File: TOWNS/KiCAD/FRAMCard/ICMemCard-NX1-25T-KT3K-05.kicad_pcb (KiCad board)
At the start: 2 copper layers, 78.5 x 47.2 mm, 19 parts, among them J1 PCMCIA_Connector, Q1 BC846X, Q2 BC846X, U1 FM18W08-SGTR, U2 FM18W08-SGTR, U3 SN74LS32DR

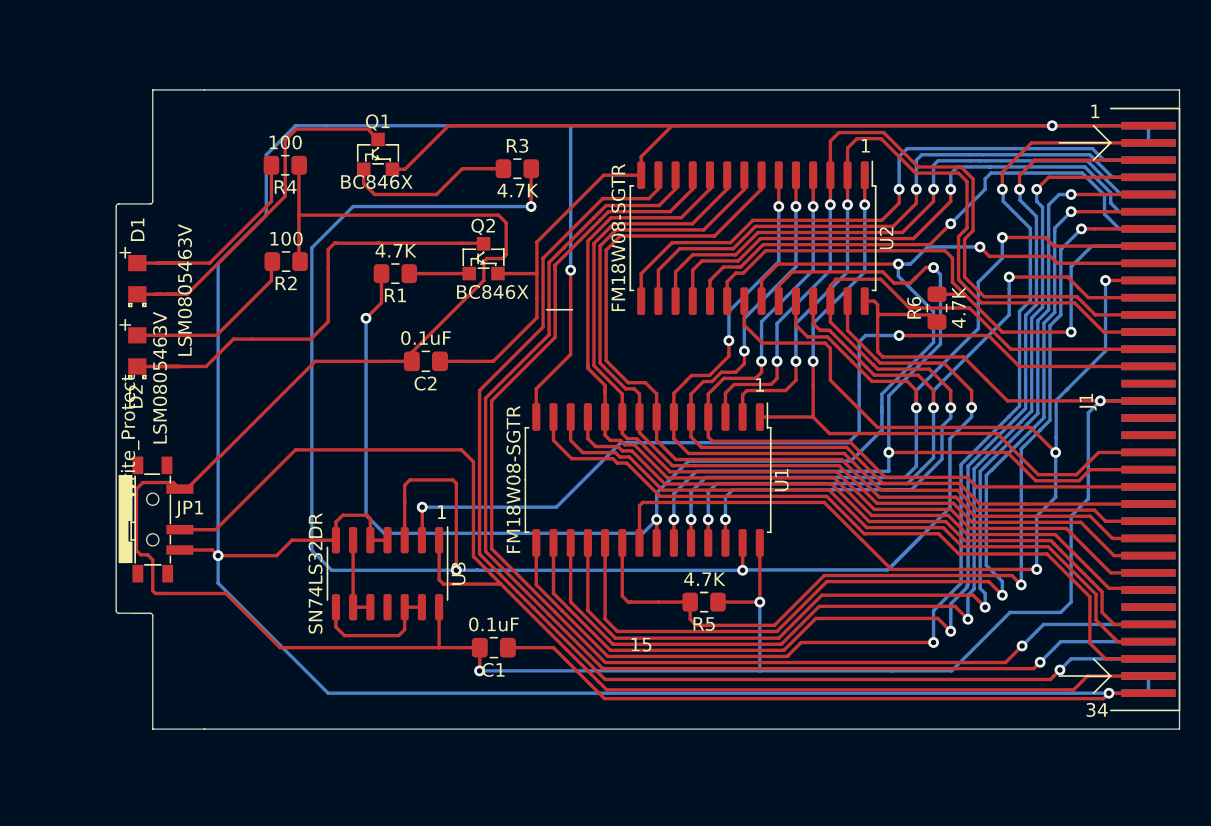
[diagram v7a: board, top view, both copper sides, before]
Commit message: Simplifying PCB
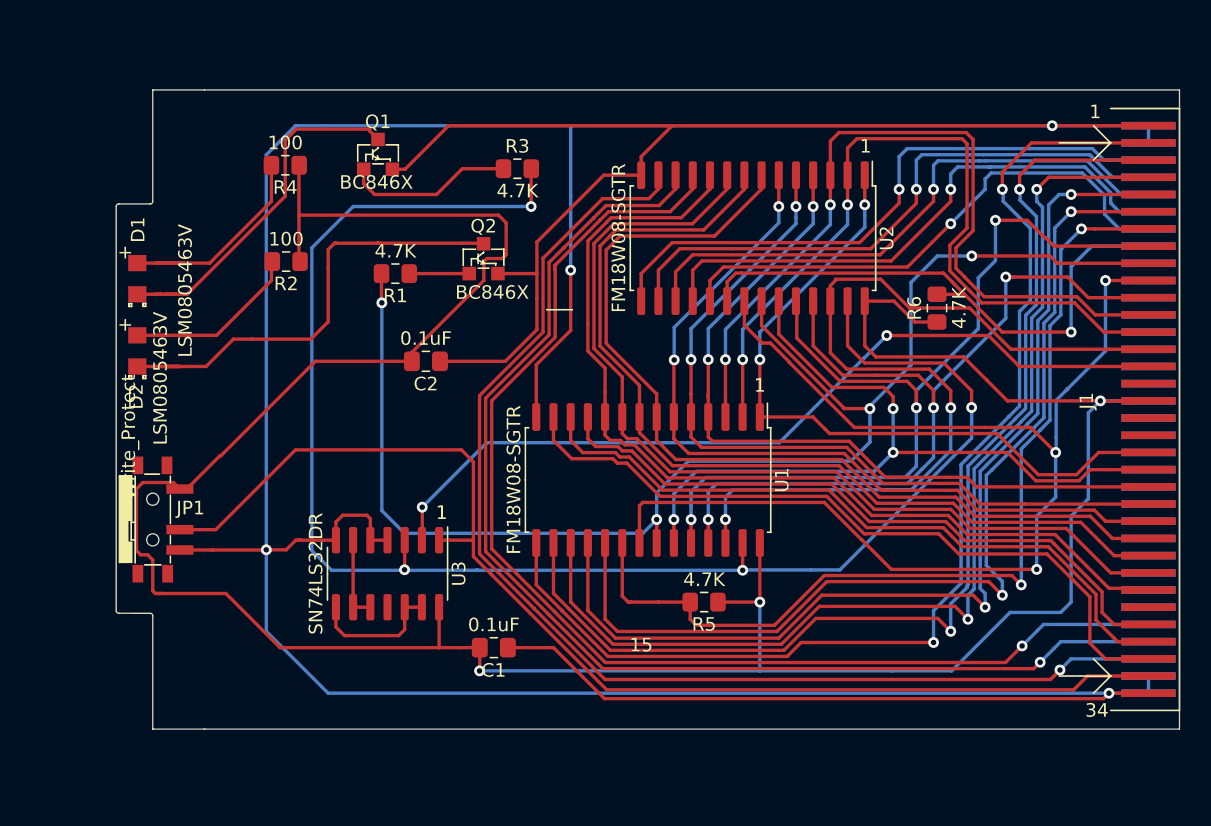
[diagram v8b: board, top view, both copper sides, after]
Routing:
- net /~WE~orWP: track 134.3 -> 117.7 mm
- net /A12: track 71.5 -> 58.0 mm
- net /~OE: track 110.0 -> 103.9 mm
- net /WP: track 93.5 -> 88.4 mm
- net /~WE: track 66.3 -> 62.4 mm
- net /A10: track 65.7 -> 68.3 mm
- net /~CE2: track 44.5 -> 42.1 mm
- net GND: track 353.1 -> 350.8 mm
- net /A15: track 50.6 -> 52.2 mm
- net /A11: track 91.1 -> 89.7 mm
- net /A14: track 65.4 -> 66.8 mm
- net Vcc: track 208.6 -> 209.8 mm
- net /A7: track 57.9 -> 56.8 mm
- net /A6: track 59.5 -> 58.5 mm
- net /A5: track 61.0 -> 60.2 mm
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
